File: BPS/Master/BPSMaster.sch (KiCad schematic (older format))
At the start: 30 parts, among them J1 SWD, J2 Logic Analyzer, J3 CurrentSlaveConnector, SW1 B3SL-1002P, U1 STM32F413RHTx, Y1 NX8045GB-8.000M-STD-CSJ-1

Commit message: Adds master board v1.1.
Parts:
- removed C12, C5, C6: 0.1uF, Capacitor_SMD:C_0805_2012Metric, symbol Device:C
- removed C53, C54: 1uF, Capacitor_SMD:C_0805_2012Metric, symbol Device:C
- removed J2: Logic Analyzer, Connector_PinHeader_2.54mm:PinHeader_2x05_P2.54mm_Vertical, symbol Connector_Generic:Conn_02x05_Odd_Even
- removed J3: CurrentSlaveConnector, UTSVT_Connectors:Molex_MicroFit3.0_1x4xP3.00mm_PolarizingPeg_Vertical, symbol Connector_Generic:Conn_01x04
- removed L5, L6: 600, Inductor_SMD:L_0805_2012Metric, symbol Device:Ferrite_Bead_Small
- removed R57, R58: 220k, Resistor_SMD:R_0805_2012Metric, symbol Device:R
- added J12: Logic Analyzer, Connector_PinHeader_2.54mm:PinHeader_2x04_P2.54mm_Vertical, symbol Connector_Generic:Conn_02x04_Odd_Even
- added J13: CAN Analyzer, Connector_PinHeader_2.54mm:PinHeader_1x03_P2.54mm_Vertical, symbol Connector_Generic:Conn_01x03
- C10: renamed from C13; value 6pF -> 10pF
- C11: renamed from C14; value 6pF -> 10pF
- J1: footprint Connector_PinHeader_2.54mm:PinHeader_1x03_P2.54mm_Vertical -> Connector_PinHeader_2.54mm:PinHeader_1x04_P2.54mm_Vertical; symbol Connector_Generic:Conn_01x03 -> Connector_Generic:Conn_01x04
- Y1: value NX8045GB-8.000M-STD-CSJ-1 -> 8M; footprint UTSVT_BPS:NX8045GB-8.000M-STD-CSJ-1 -> Crystal:Crystal_SMD_TXC_7A-2Pin_5x3.2mm; P/N (none) -> CRYSTAL 8.0000MHZ 18PF SMD
- renumbered C7 to C5, C9 to C6, C10 to C7, C11 to C8, C8 to C9
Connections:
- net labels added: SPI3_CLK, SPI3_MISO, SPI3_MOSI, USART3_RX, USART3_TX, VOLT_CS
- net labels removed: DISPLAY_CS, LTC6811_CS, PC4, PC5, UART1_RX, UART1_TX
- wire segments 199 -> 159
- no-connect marks 13 -> 14
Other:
- note added: "The crystal and caps have to be as \nclose to the uC as possible."
- note removed: "- Display\n- Volt Slave\n- Temp Slave"
- note removed: "- EEPROM\n- IMU"
- note removed: "Current Board"
- note removed: "Debug"
- note removed: "PA2 high precision hall effect sensor.\nPA3 low precision hall effect sensor."
- note removed: "The crystal and caps have to be as close to the uC as possible."
- moved on the sheet: C10, C11, C5, C9, U1, Y1

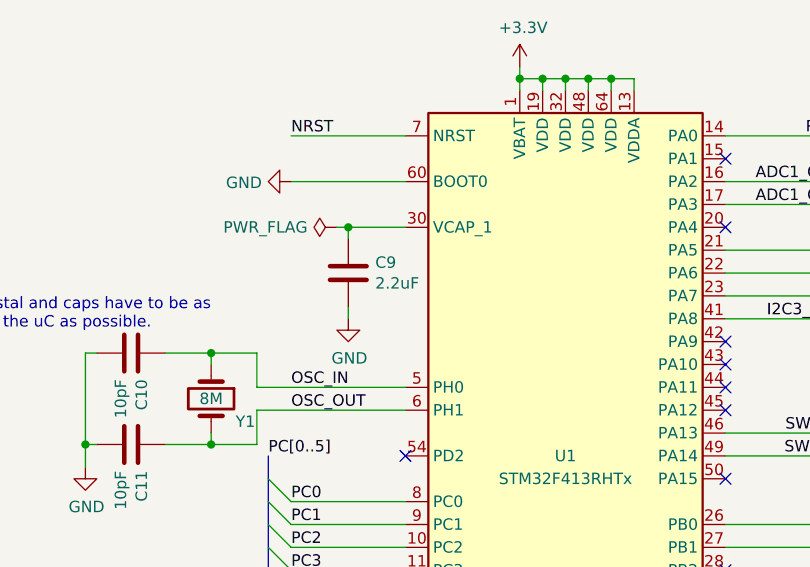
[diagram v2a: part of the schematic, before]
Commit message: Change capacitor value for VCAP on master board to 4.7uF
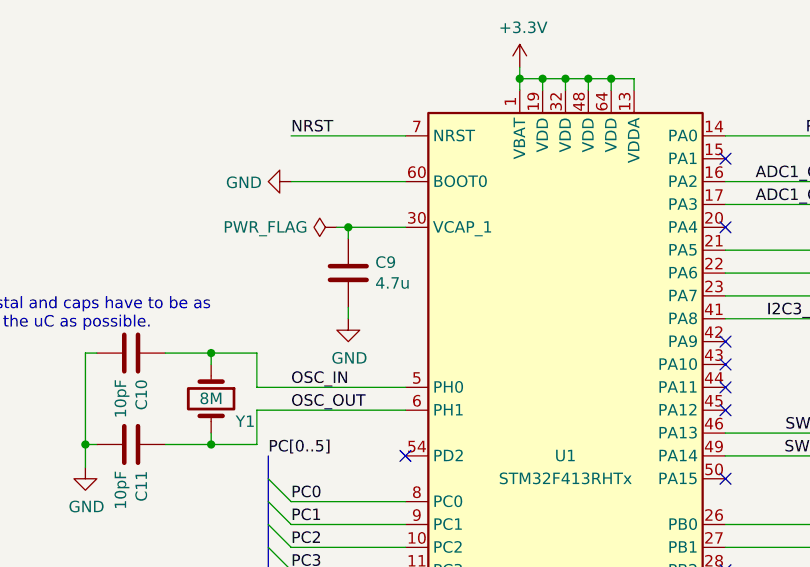
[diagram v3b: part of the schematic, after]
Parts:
- C9: value 2.2uF -> 4.7u
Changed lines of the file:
@@
 P 4850 3000
 F 0 "C9" H 4968 3046 50  0000 L CNN
-F 1 "2.2uF" H 4968 2955 50  0000 L CNN
+F 1 "4.7u" H 4968 2955 50  0000 L CNN
 F 2 "Capacitor_SMD:C_0805_2012Metric" H 4888 2850 50  0001 C CNN
 F 3 "~" H 4850 3000 50  0001 C CNN

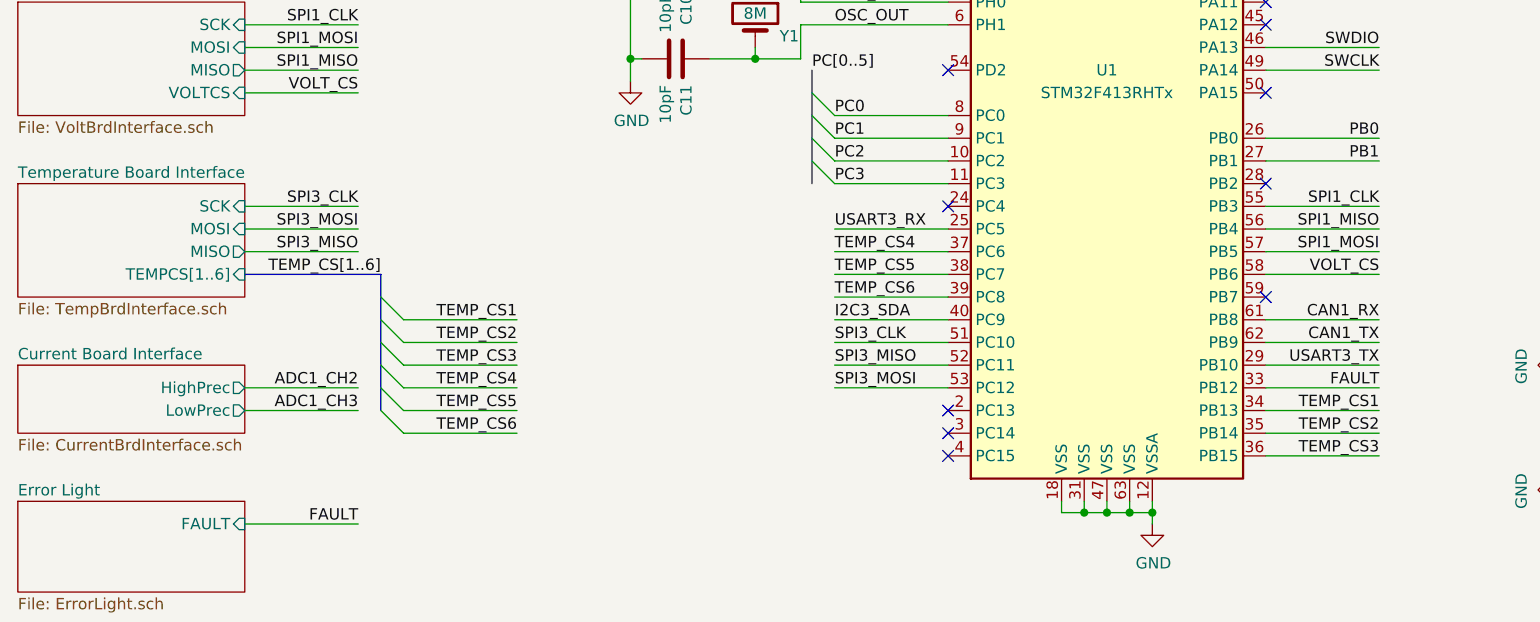
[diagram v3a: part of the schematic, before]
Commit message: Edits master board to not have temperature board pinouts.
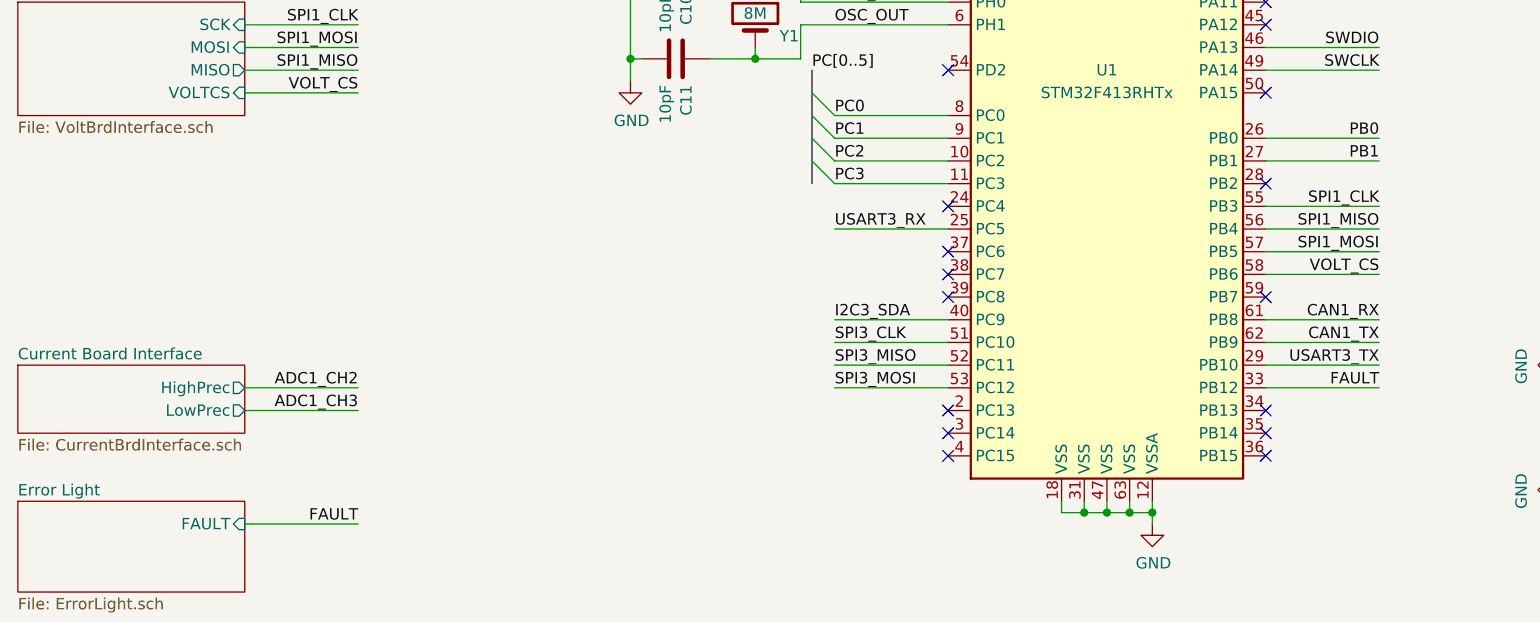
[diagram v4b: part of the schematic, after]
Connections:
- net TEMP_CS1: no longer names the net of U1.34 (PB13)
- net TEMP_CS2: no longer names the net of U1.35 (PB14)
- net TEMP_CS3: no longer names the net of U1.36 (PB15)
- net TEMP_CS4: no longer names the net of U1.37 (PC6)
- net TEMP_CS5: no longer names the net of U1.38 (PC7)
- net TEMP_CS6: no longer names the net of U1.39 (PC8)
- no-connect marks 14 -> 20
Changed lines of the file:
@@
 $Descr A4 11693 8268
 encoding utf-8
-Sheet 1 11
+Sheet 1 10
 Title ""
 Date ""
@@
 Text Label 4500 3800 0    50   ~ 0
 PC[0..5]
-Entry Wire Line
-	2700 5400 2600 5300
-Entry Wire Line
-	2700 5300 2600 5200
-Entry Wire Line
-	2700 5200 2600 5100
-Entry Wire Line
-	2700 5100 2600 5000
-Entry Wire Line
-	2700 5000 2600 4900
-Entry Wire Line
-	2700 4900 2600 4800
 Text Label 2500 7000 2    50   ~ 0
 PC[0..5]
@@
 	4800 2800 4850 2800
 Connection ~ 4850 2800
-Wire Wire Line
-	6500 5300 7000 5300
-Wire Wire Line
-	6500 5400 7000 5400
-Wire Wire Line
-	6500 5500 7000 5500
-Text Label 7000 5300 2    50   ~ 0
-TEMP_CS1
-Text Label 7000 5400 2    50   ~ 0
-TEMP_CS2
-Text Label 7000 5500 2    50   ~ 0
-TEMP_CS3
-Wire Wire Line
-	4600 4600 5100 4600
-Text Label 4600 4600 0    50   ~ 0
-TEMP_CS4
-Wire Wire Line
-	4600 4700 5100 4700
-Wire Wire Line
-	5100 4800 4600 4800
-Text Label 4600 4700 0    50   ~ 0
-TEMP_CS5
-Text Label 4600 4800 0    50   ~ 0
-TEMP_CS6
 NoConn ~ 6500 3500
 NoConn ~ 6500 3600
@@
 Wire Wire Line
 	6500 5100 7000 5100
-$Sheet
-S 1000 4300 1000 500
-U 5D7654E1
-F0 "Temperature Board Interface" 50
-F1 "TempBrdInterface.sch" 50
-F2 "TEMPCS[1..6]" I R 2000 4700 50
-F3 "SCK" I R 2000 4400 50
-F4 "MOSI" I R 2000 4500 50
-F5 "MISO" O R 2000 4600 50
-$EndSheet
 Wire Wire Line
 	2000 3600 2500 3600
@@
 F3 "CAN_RX" O R 2000 1900 50
 $EndSheet
-Text Label 2500 4500 2    50   ~ 0
-SPI3_MOSI
-Text Label 2500 4600 2    50   ~ 0
-SPI3_MISO
-Text Label 2500 4400 2    50   ~ 0
-SPI3_CLK
-Wire Wire Line
-	2000 4600 2500 4600
-Wire Wire Line
-	2500 4500 2000 4500
-Wire Wire Line
-	2000 4400 2500 4400
-Text Label 2600 4700 2    50   ~ 0
-TEMP_CS[1..6]
-Wire Bus Line
-	2000 4700 2600 4700
-Text Label 3200 5400 2    50   ~ 0
-TEMP_CS6
-Text Label 3200 5300 2    50   ~ 0
-TEMP_CS5
-Text Label 3200 5200 2    50   ~ 0
-TEMP_CS4
-Text Label 3200 5100 2    50   ~ 0
-TEMP_CS3
-Text Label 3200 5000 2    50   ~ 0
-TEMP_CS2
-Wire Wire Line
-	2700 5400 3200 5400
-Text Label 3200 4900 2    50   ~ 0
-TEMP_CS1
-Wire Wire Line
-	3200 5300 2700 5300
-Wire Wire Line
-	3200 5200 2700 5200
-Wire Wire Line
-	3200 5100 2700 5100
-Wire Wire Line
-	3200 5000 2700 5000
-Wire Wire Line
-	3200 4900 2700 4900
 $Sheet
 S 1000 5700 1000 400
@@
 Text Label 7800 5850 0    50   ~ 0
 CAN1_TX
+NoConn ~ 5100 4600
+NoConn ~ 5100 4700
+NoConn ~ 5100 4800
+NoConn ~ 6500 5300
+NoConn ~ 6500 5400
+NoConn ~ 6500 5500
 Wire Bus Line
 	7100 2700 7100 3000
 Wire Bus Line
 	4500 3800 4500 4300
-Wire Bus Line
-	2600 4700 2600 5300
 $EndSCHEMATC
